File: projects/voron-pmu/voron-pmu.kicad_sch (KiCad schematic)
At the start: 17 parts, among them J1 Critical loads, J2 Non-critical loads, J3 Critical supply, J4 Non-critical supply, J5 Pwr-loss-1, J6 Pwr-loss-2, K1 G2RL-2, K2 G2RL-2, K3 G2RL-2, K4 FINDER-40.52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

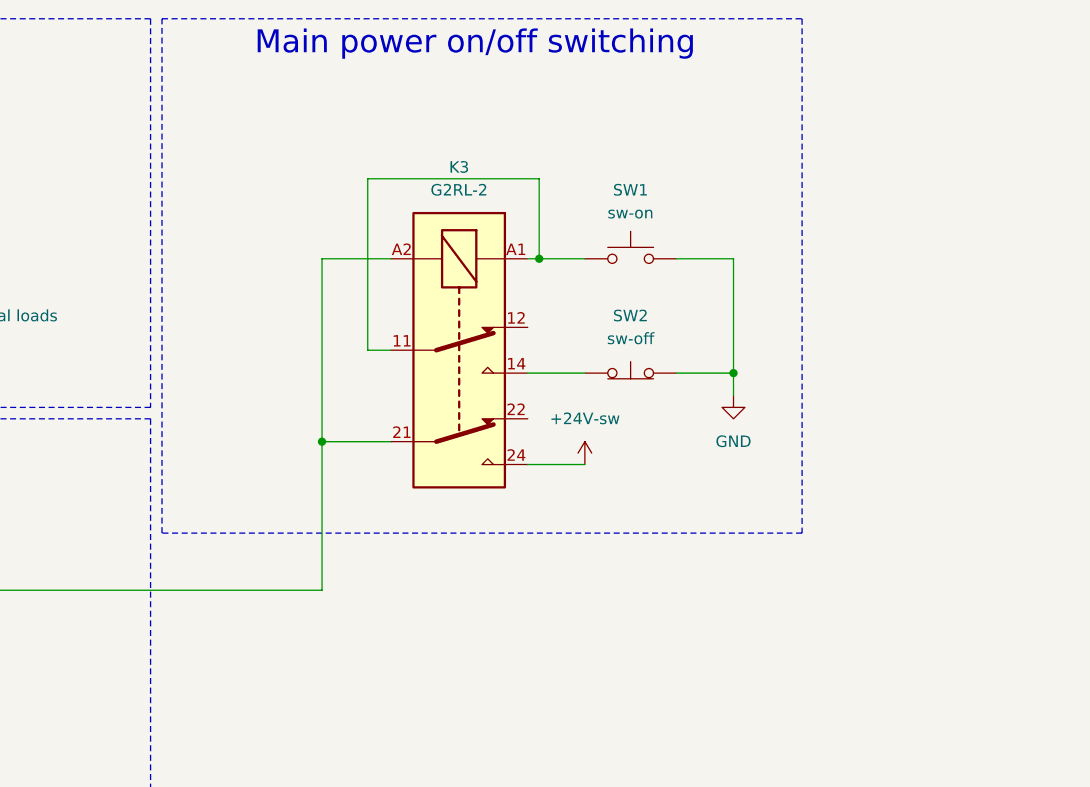
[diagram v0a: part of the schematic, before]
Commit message: Adding pwr-good and stby indications.
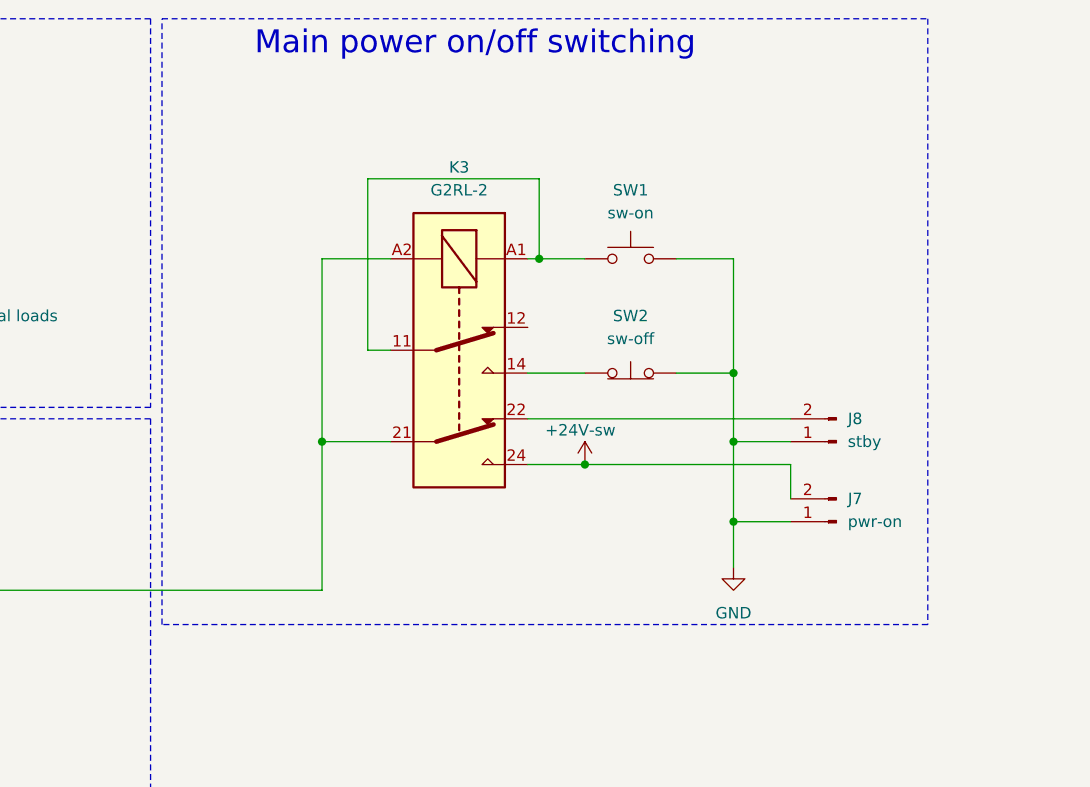
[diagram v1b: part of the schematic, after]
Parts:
- added J7: pwr-on, Connector_JST:JST_XH_B2B-XH-A_1x02_P2.50mm_Vertical, symbol Connector:Conn_01x02_Pin
- added J8: stby, Connector_JST:JST_XH_B2B-XH-A_1x02_P2.50mm_Vertical, symbol Connector:Conn_01x02_Pin
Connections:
- net +24V-sw: now also J7.2 (Pin_2)
- net GND: now also J7.1 (Pin_1), J8.1 (Pin_1)
- net at K3.22: now also J8.2 (Pin_2)

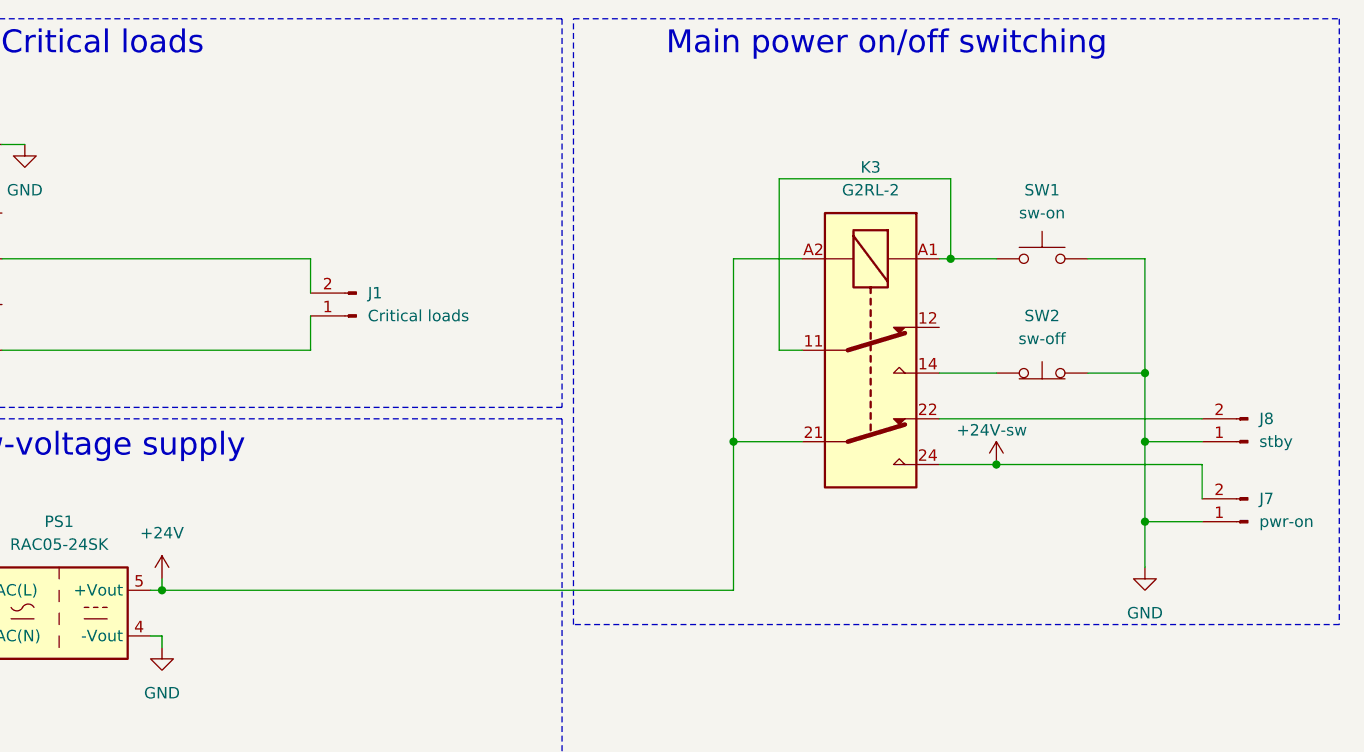
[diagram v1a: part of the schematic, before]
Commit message: Moving on/off switches to the high side.
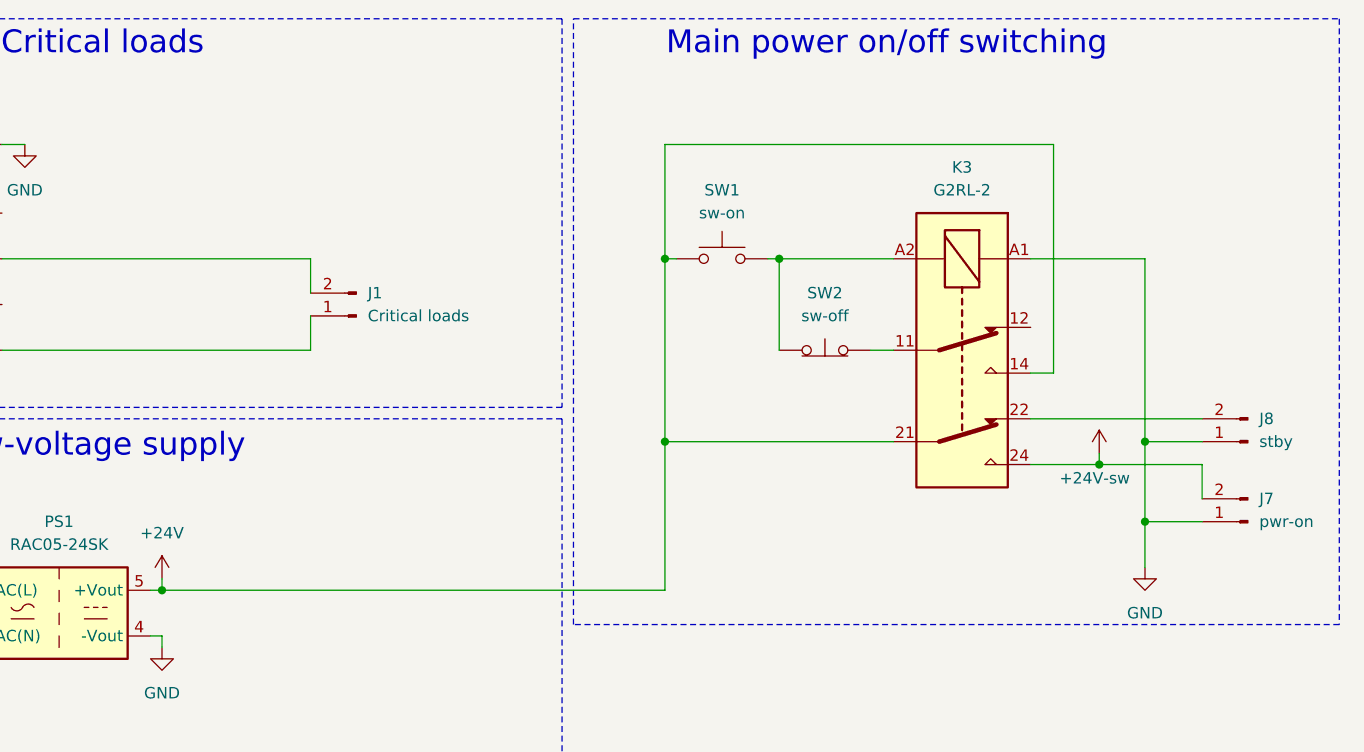
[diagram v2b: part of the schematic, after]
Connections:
- net +24V: now also K3.14, SW1.1; no longer K3.A2
- net GND: now also K3.A1; no longer SW1.2, SW2.2 (B)
- net at SW2.1 (A): now also K3.A2, SW1.2; no longer K3.14
- new net: K3.11, SW2.2 (B)
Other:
- moved on the sheet: K3, SW1, SW2

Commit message: Routing a new revision.
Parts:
- PS1: footprint Converter_ACDC:Converter_ACDC_RECOM_RAC05-xxSK_THT -> Converter_ACDC:Converter_ACDC_RECOM_RAC04-xxSGx_THT; symbol Converter_ACDC:RAC05-24SK -> Converter_ACDC:RAC04-24SGA
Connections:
- net neutral-non-critical: now reaches K2.14, K4.A1
- net neutral-non-critical: now also J2.1 (Pin_1); no longer J2.2 (Pin_2)
- net line-non-critical: now reaches K2.24, K4.A2
- net line-non-critical: now also J2.2 (Pin_2); no longer J2.1 (Pin_1)
- net line-in: now reaches J3.2 (Pin_2), K1.21, PS1.1 (AC(L))
- net neutral-in: now reaches J3.1 (Pin_1), K1.11, PS1.2 (AC(N))
- net neutral-in-aux: now reaches J4.1 (Pin_1), K2.11
- net line-in-aux: now reaches J4.2 (Pin_2), K2.21
- net line-critical: now reaches J1.2 (Pin_2)
- net line-critical: now also K1.24; no longer K1.14
- net neutral-critical: now reaches J1.1 (Pin_1)
- net neutral-critical: now also K1.14; no longer K1.24
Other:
- moved on the sheet: J1, J2
